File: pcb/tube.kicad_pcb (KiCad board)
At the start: 2 copper layers, 99.1 x 116.8 mm, 83 parts, among them J1 Screw_Terminal_01x02, J10 LED_[5..8], J11 LED_[1..4], J2 Screw_Terminal_01x02, J3 Screw_Terminal_01x02, J4 Conn_01x04_Pin, J5 Conn_01x10_Pin, J6 Conn_01x05_Pin, U1 INA226, U10 74LS32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

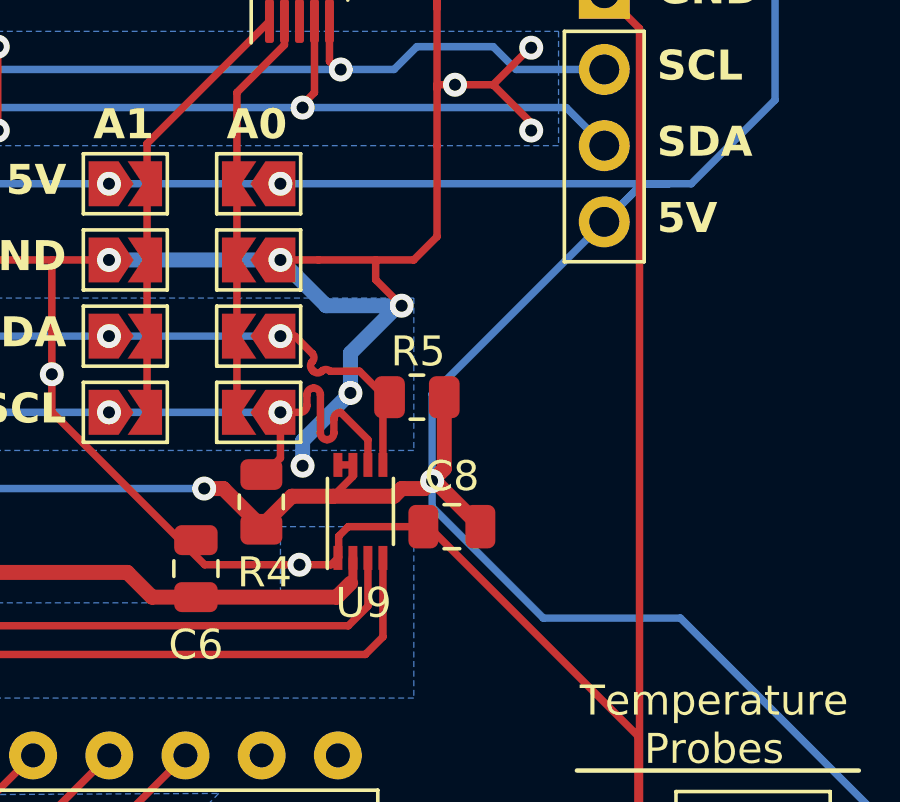
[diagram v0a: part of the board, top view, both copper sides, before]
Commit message: PCB: Fulfill PCA9306 Spec
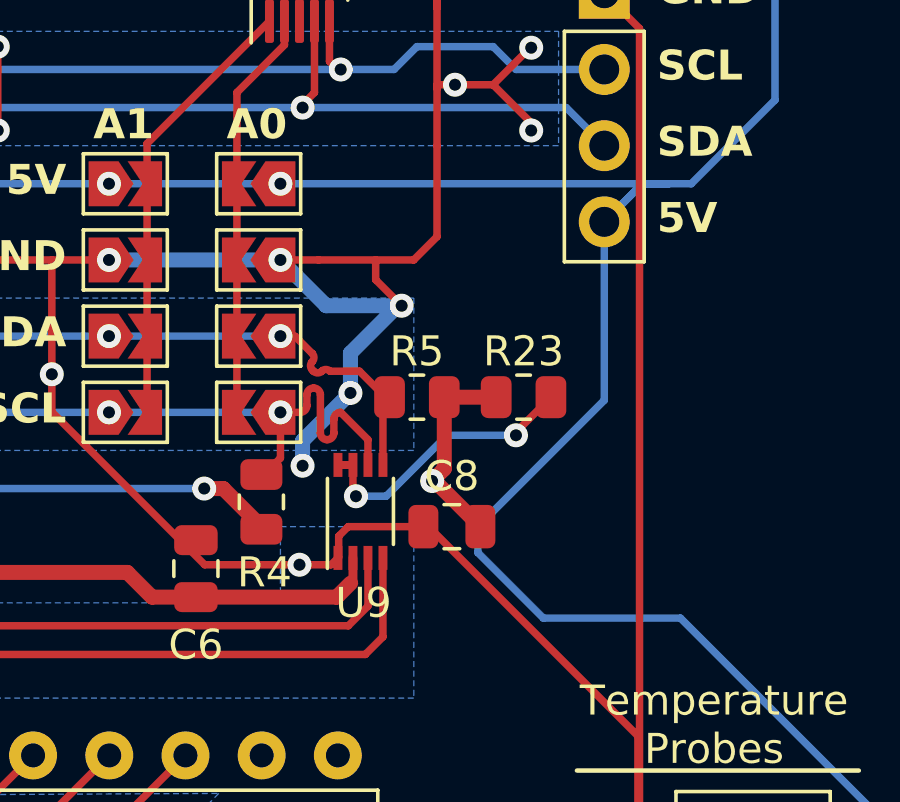
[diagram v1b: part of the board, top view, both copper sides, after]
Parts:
- added R23: 200kΩ, Resistor_SMD:R_0805_2012Metric, F.Cu at (227.3, 150.1)
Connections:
- U9 pad 7: +5V -> Net-(U9-EN)
- U9 pad 8: +5V -> Net-(U9-EN)
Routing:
- net Net-(U9-EN): track 0.00 -> 10.4 mm, vias 0 -> 2
- net +5V: track 561.8 -> 556.8 mm

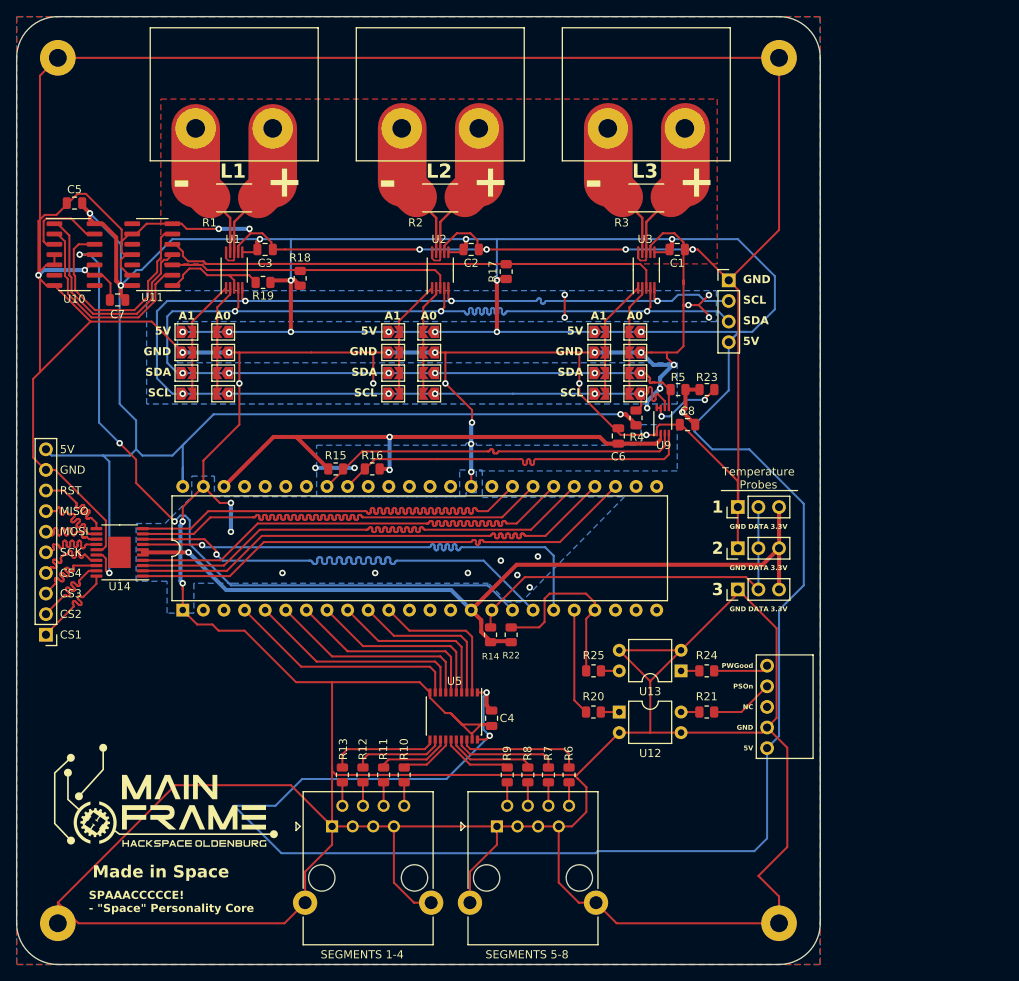
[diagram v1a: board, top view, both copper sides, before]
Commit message: PCB: Add TODO notices
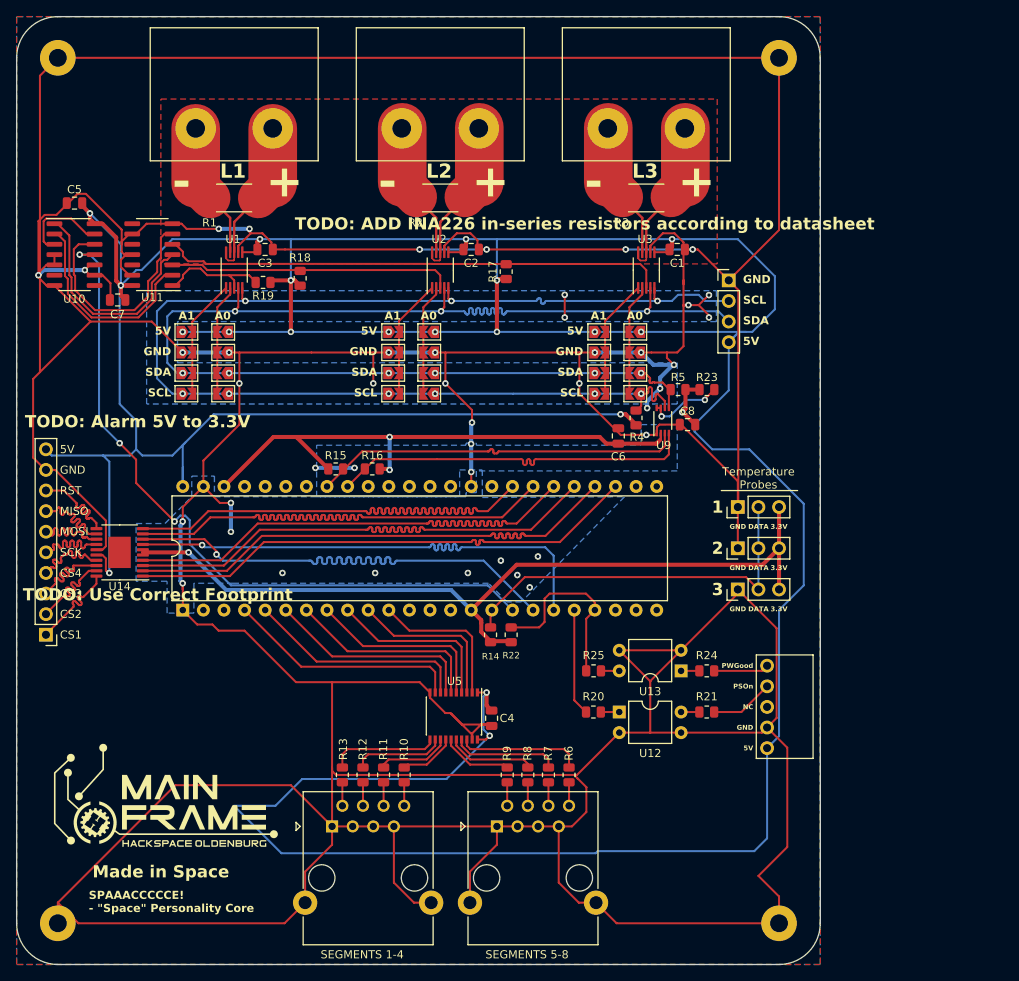
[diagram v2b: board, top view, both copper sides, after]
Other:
- board text added: "TODO: ADD INA226 in-series resistors according to datasheet"
- board text added: "TODO: Alarm 5V to 3.3V"
- board text added: "TODO: Use Correct Footprint"
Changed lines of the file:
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@@
     (effects (font (size 1 1) (thickness 0.15)) (justify left))
+  )
+  (gr_text "TODO: Use Correct Footprint" (at 143.002 176.276) (layer "F.SilkS")
+    (effects (font (size 1.5 1.5) (thickness 0.3) bold) (justify left bottom))
   )
   (gr_text "MISO\n" (at 147.574 165.1) (layer "F.SilkS")
@@
   (gr_text "+" (at 226.06 124.46) (layer "F.SilkS")
     (effects (font (size 4 4) (thickness 1) bold))
+  )
+  (gr_text "TODO: Alarm 5V to 3.3V" (at 143.256 154.94) (layer "F.SilkS")
+    (effects (font (size 1.5 1.5) (thickness 0.3) bold) (justify left bottom))
   )
   (gr_text "GND" (at 212.09 145.415) (layer "F.SilkS")
@@
     (effects (font (size 1 1) (thickness 0.2) bold) (justify bottom))
   )
+  (gr_text "TODO: ADD INA226 in-series resistors according to datasheet" (at 176.53 130.556) (layer "F.SilkS")
+    (effects (font (size 1.5 1.5) (thickness 0.3) bold) (justify left bottom))
+  )
   (gr_text "3.3V" (at 236.22 167.005) (layer "F.SilkS")
